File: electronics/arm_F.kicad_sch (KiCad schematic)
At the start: 26 parts, among them J12 EV3 F 4434 HOLD, J22 F SERVO G + S, U12 DRV8871DDAR, U22 SN74LVC2G17DBVR, U32 SN74AHCT1G125DBVR

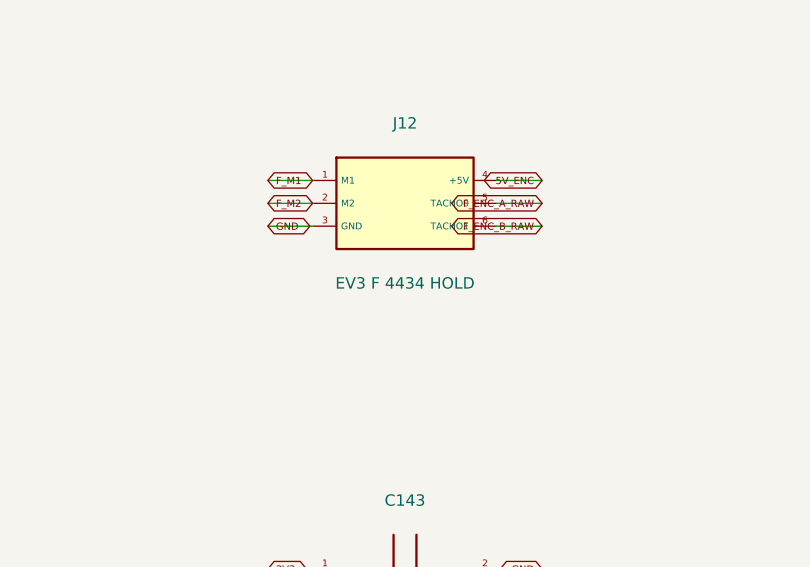
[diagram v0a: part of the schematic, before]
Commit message: Integrate onboard RP2040 and drawing-based EV3 jacks on A1 PCB
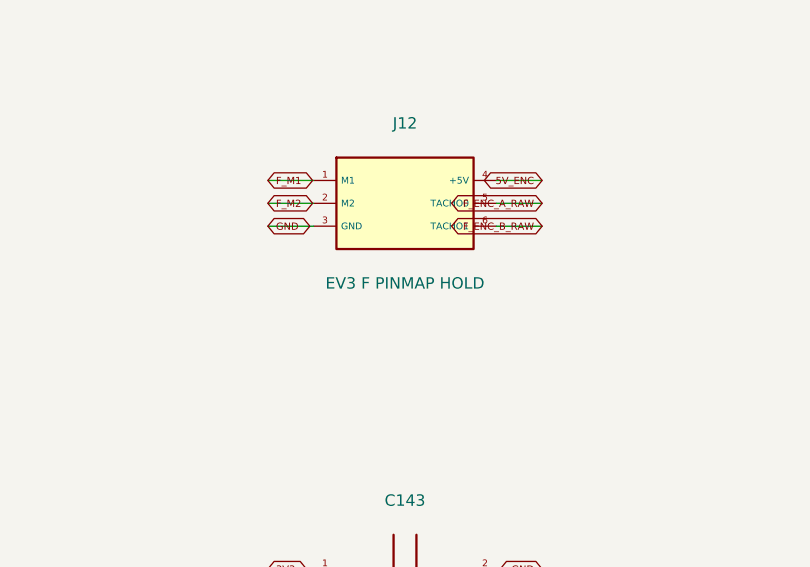
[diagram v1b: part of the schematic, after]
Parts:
- J12: value EV3 F 4434 HOLD -> EV3 F PINMAP HOLD; footprint Quadcuber:EV3_4434_PROVISIONAL -> Quadcuber:EV3_UserDrawing_PINMAP_HOLD; MPN 4434 -> UNCONFIRMED user drawing; Manufacturer Adafruit (supplier brand) -> Unconfirmed (Coorle watermark)
- TP18, TP19, TP20, TP21: now left out of the parts list
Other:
- title: Quadcuber A0 / arm_F / ENGINEERING HOLD -> Quadcuber A1 / arm_F / ENGINEERING HOLD

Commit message: Correct audited power BOM and add bounded VM discharge protection
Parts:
- C141: MPN GRM32ER71E106KA12L -> GRM32DR71E106KA12L
- F12: footprint Quadcuber:Fuse_1812_4532Metric -> Quadcuber:Fuse_Bourns_MF_MSMF_Style2_1812; MPN MF-MSMF110-2 -> MF-MSMF110/16X-2

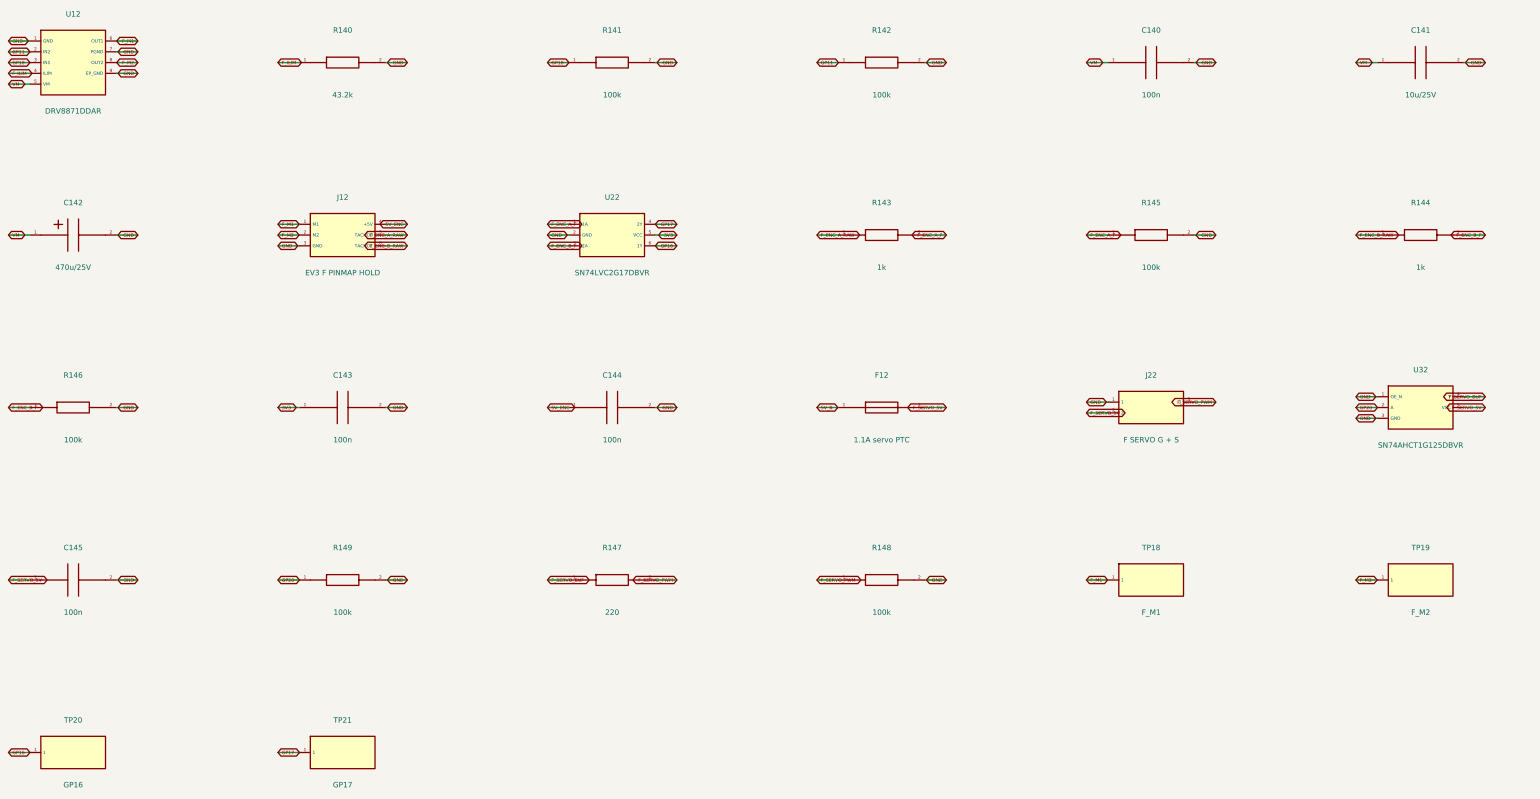
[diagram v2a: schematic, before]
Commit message: Migrate A1 to KiCad 10 and record blocked vendor-model transients
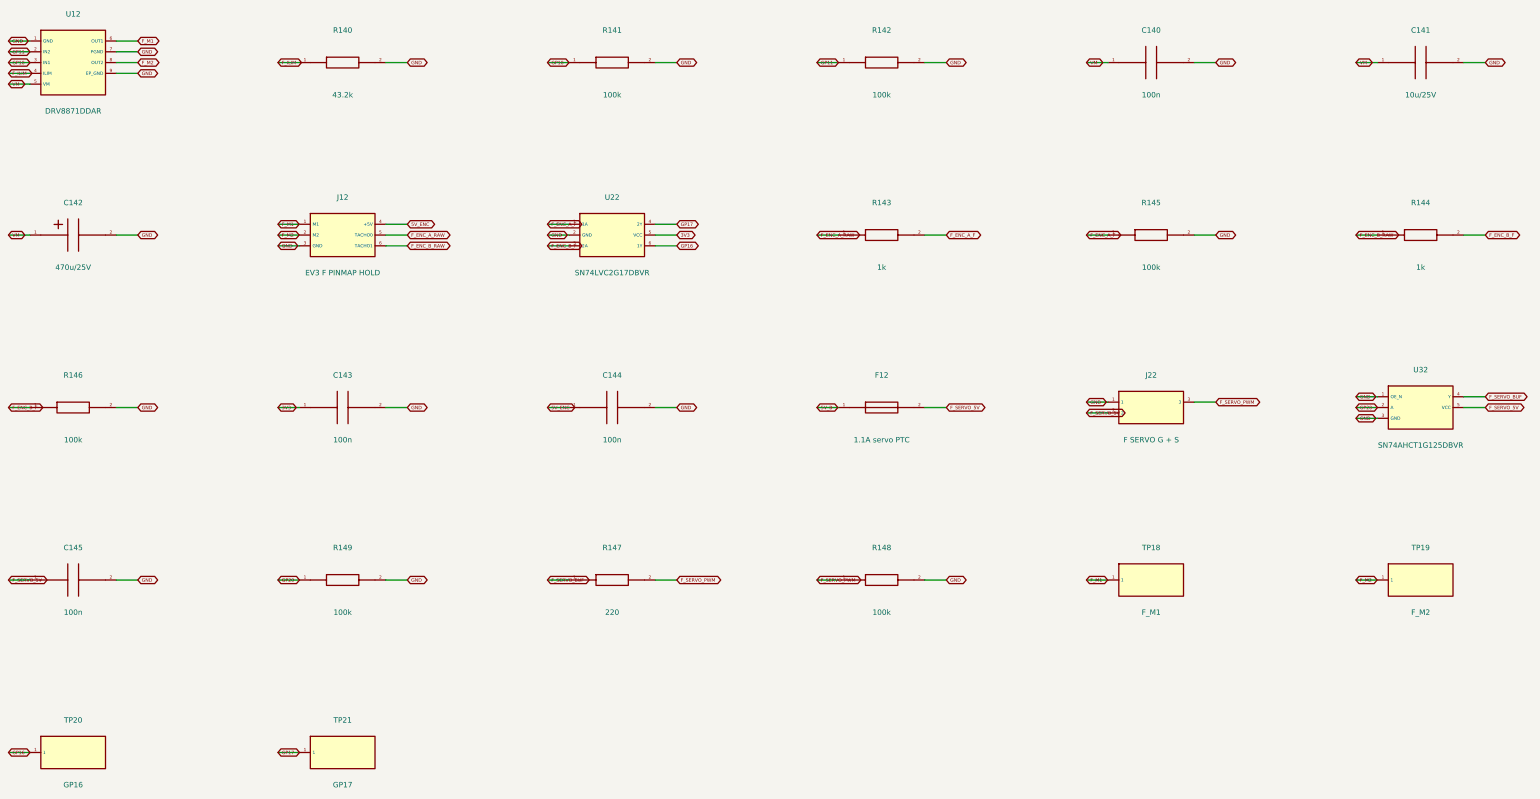
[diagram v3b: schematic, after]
